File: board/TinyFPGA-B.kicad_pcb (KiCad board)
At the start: 2 copper layers, 17.8 x 35.6 mm, 36 parts, among them J1 CONN_01X14, J2 CONN_01X14, J3 USB_OTG, SW1 SW_Push, U1 iCE40-LP8K-CM81, U2 MIC5504-3.3YM5-TR, U3 DSC6001CI2A-016.0000T, U4 MIC5365-1.2YC5-TR, U5 AT25SF041-SSHD-B

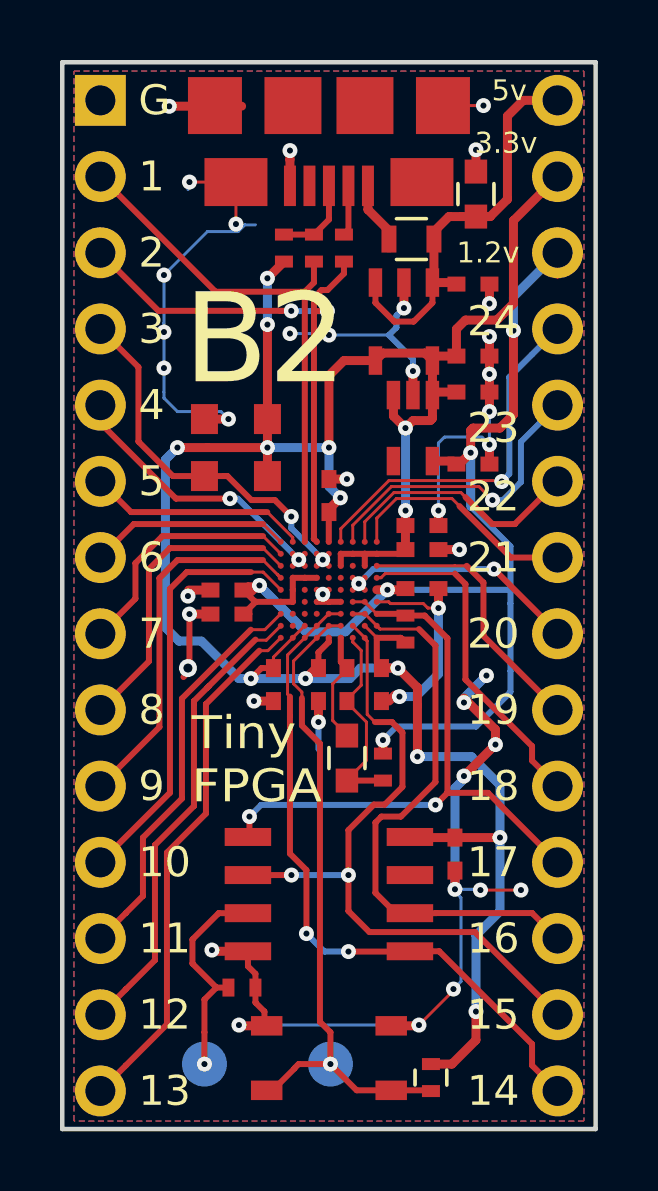
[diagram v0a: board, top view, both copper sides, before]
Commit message: added template iCEcube2 project to use as starting point for user designs
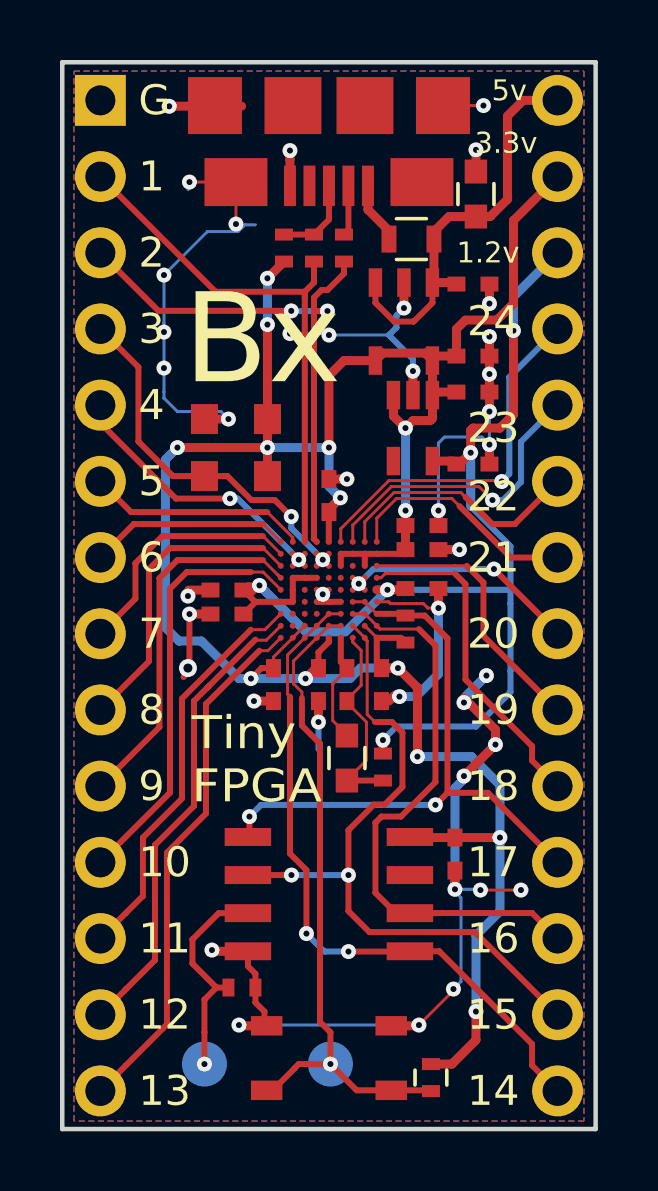
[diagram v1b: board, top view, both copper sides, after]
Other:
- board text added: "Bx"
- board text removed: "B2"
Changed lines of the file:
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@@
     (links 150)
     (no_connects 0)
-    (area 142.164999 96.444999 160.095001 132.155001)
+    (area 138.476667 92.439 163.783334 134.215)
     (thickness 1.6)
     (drawings 62)
@@
     (34 B.Paste user)
     (35 F.Paste user)
-    (36 B.SilkS user hide)
+    (36 B.SilkS user)
     (37 F.SilkS user)
     (38 B.Mask user)
@@
     (effects (font (size 1.1 1.2) (thickness 0.275)) (justify left))
   )
-  (gr_text B2 (at 146.28 105.764) (layer F.SilkS)
+  (gr_text Bx (at 146.28 105.764) (layer F.SilkS)
     (effects (font (size 3 3) (thickness 0.5)) (justify left))
   )
